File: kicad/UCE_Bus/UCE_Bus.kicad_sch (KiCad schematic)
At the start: 1 part, among them J1 SODIMM-200

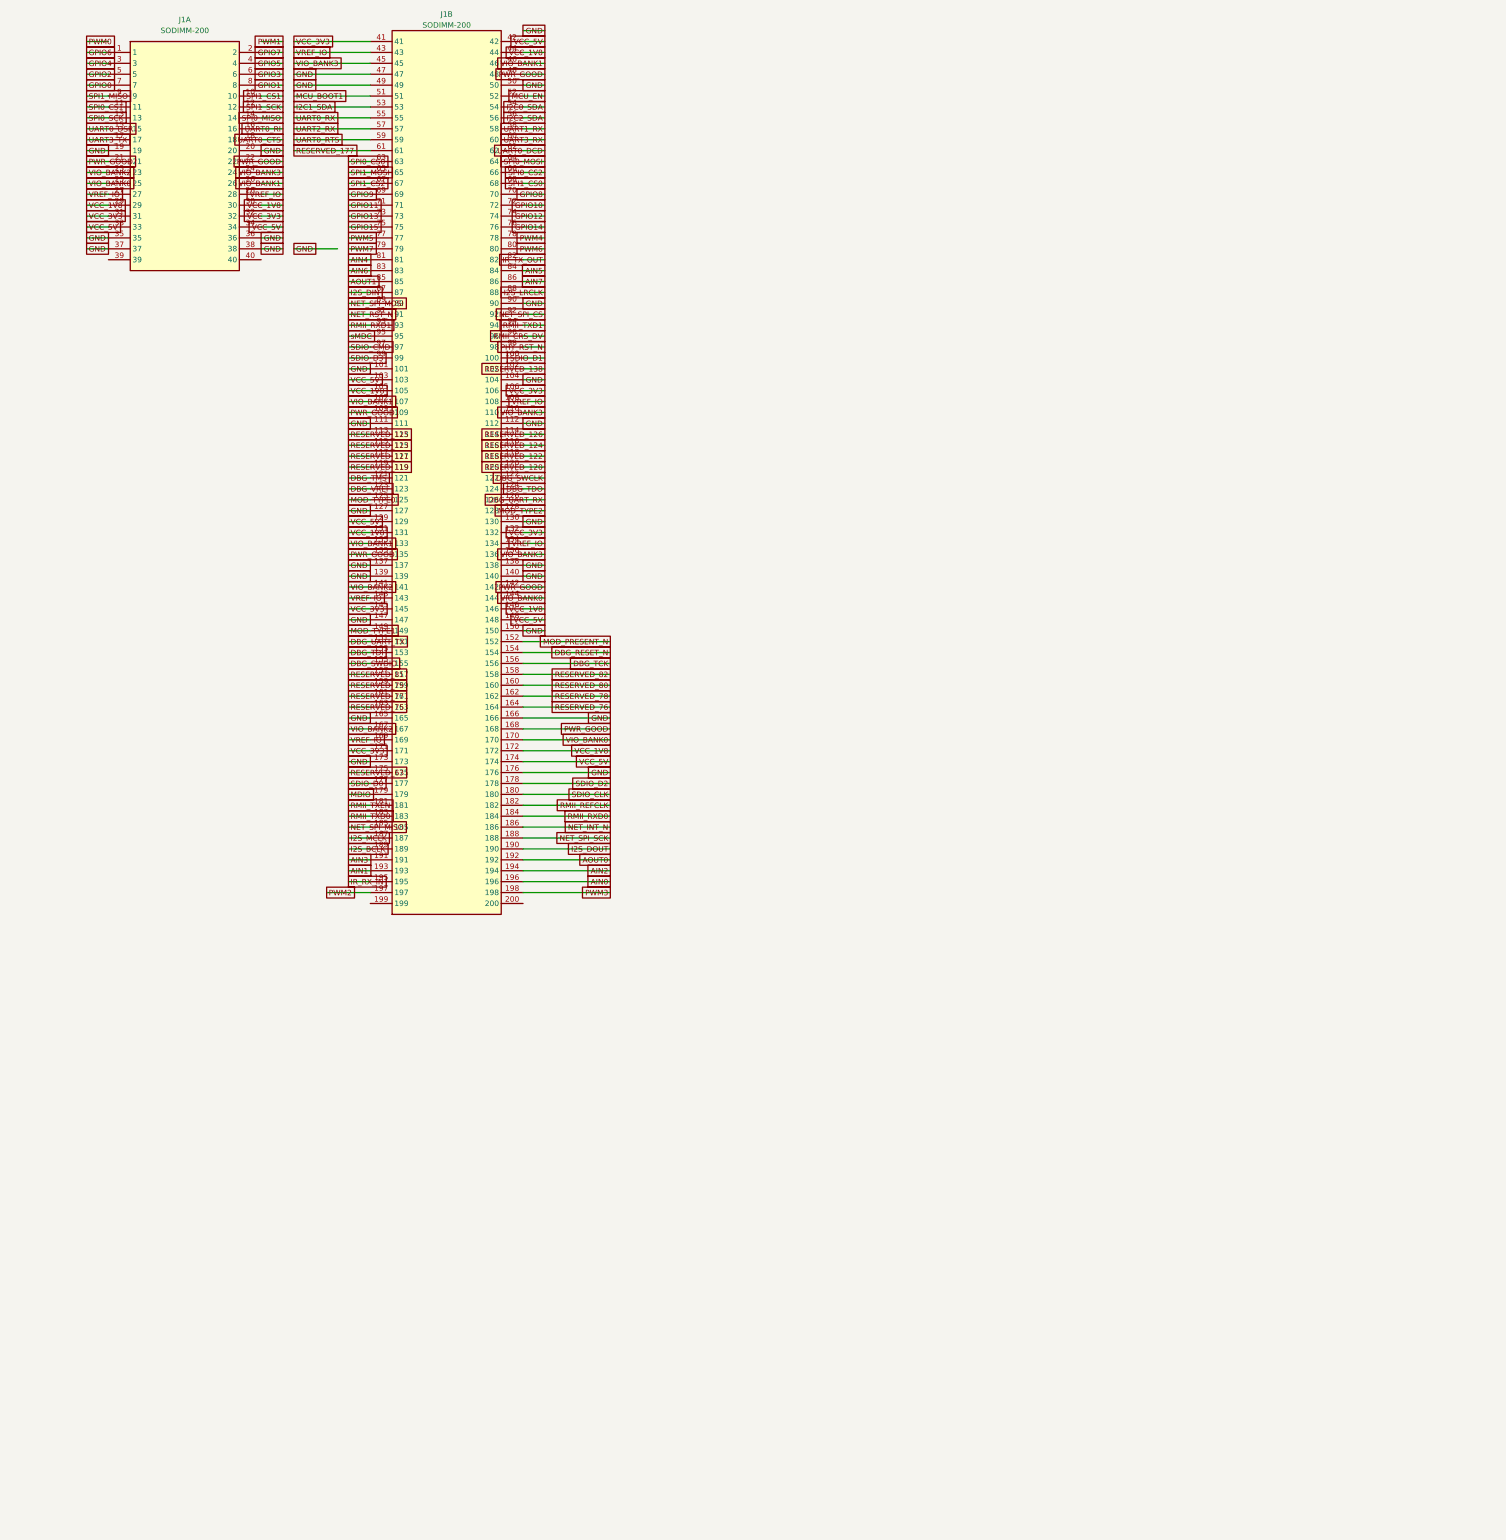
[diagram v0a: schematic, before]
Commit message: Finalizado versão 0.4 do conector do UCE para o módulo.
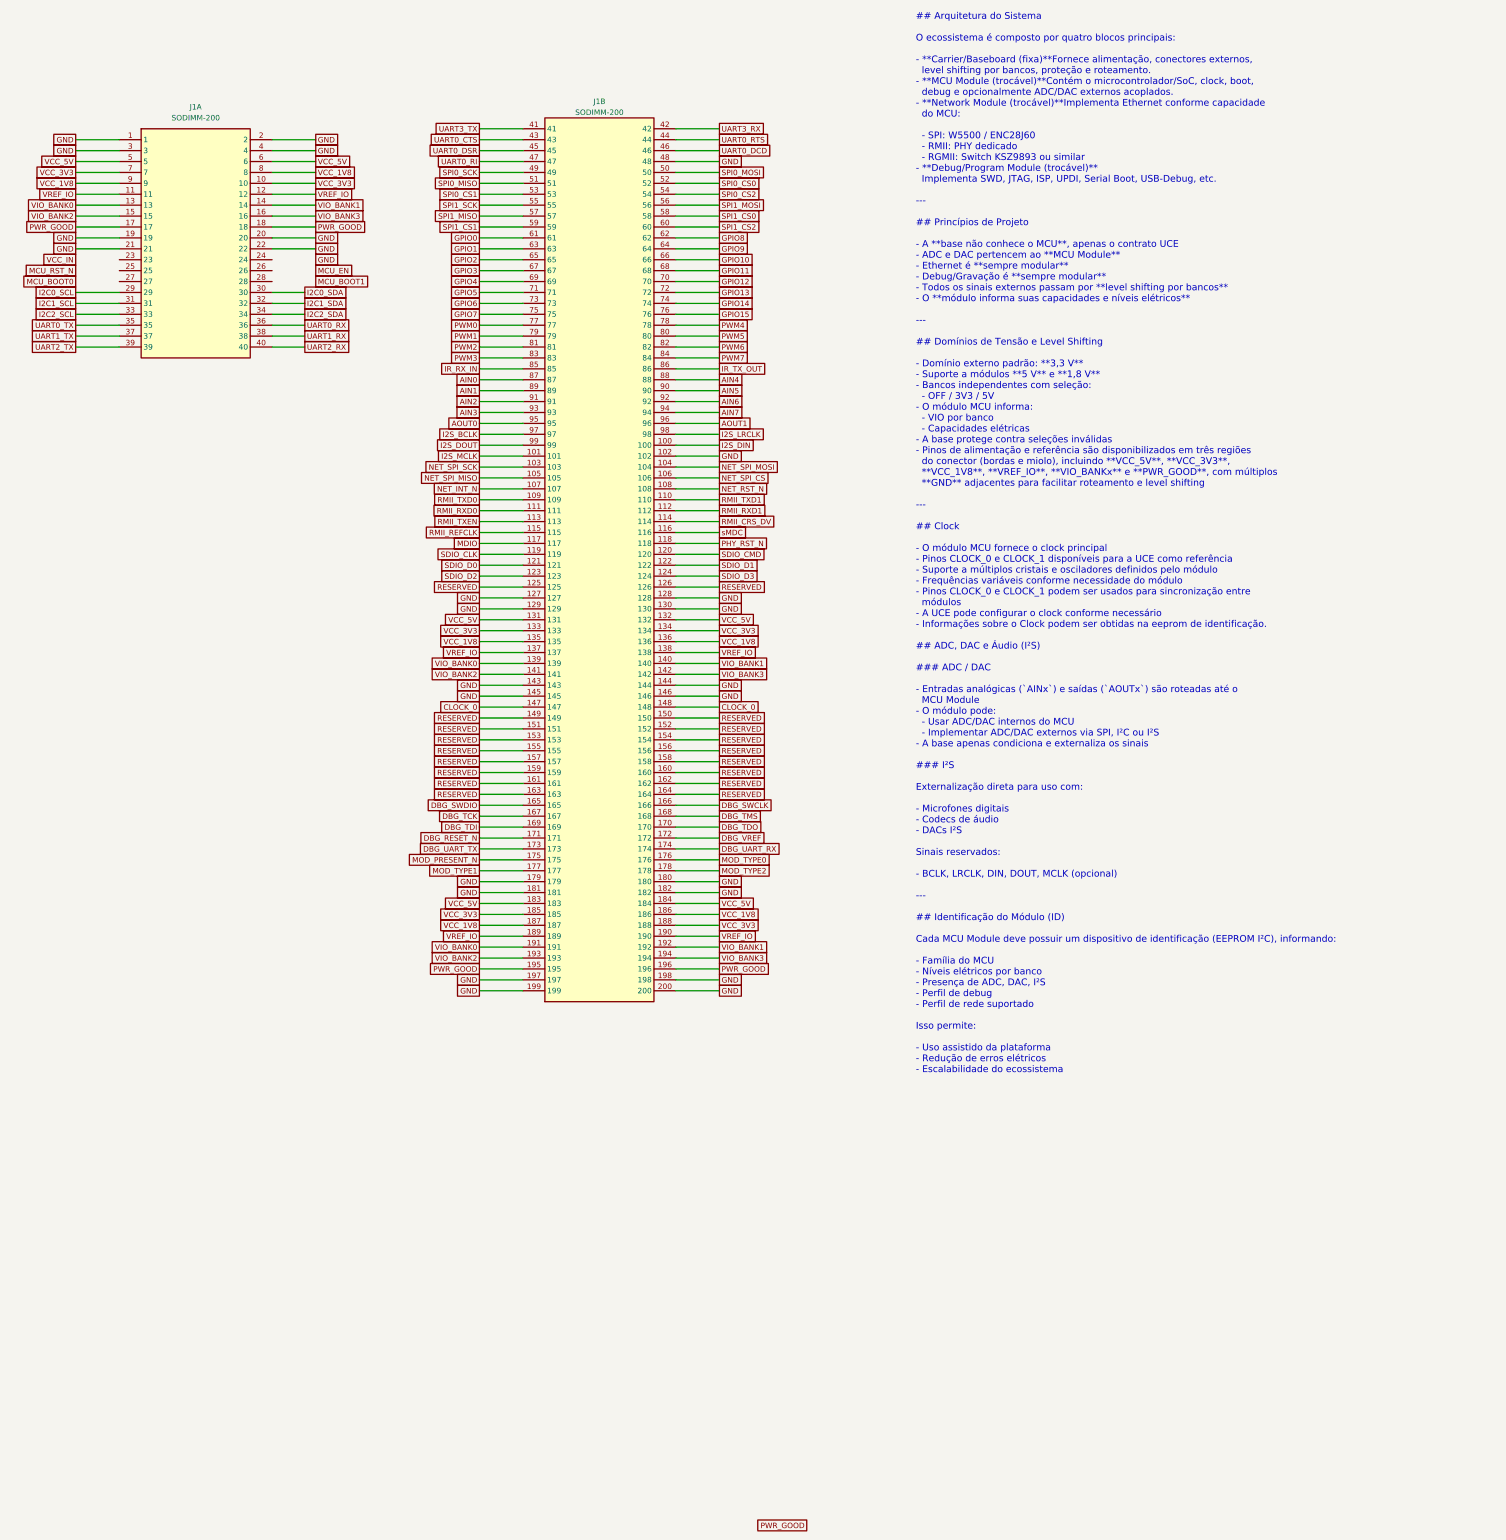
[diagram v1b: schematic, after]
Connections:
- net RESERVED_119 is gone; now on net SDIO_CLK: J1.119
- net RESERVED_120 is gone; now on net SDIO_CMD: J1.120
- net RESERVED_121 is gone; now on net MDIO: J1.117
- net RESERVED_122 is gone; now on net PHY_RST_N: J1.118
- net RESERVED_123 is gone; now on net RMII_REFCLK: J1.115
- net RESERVED_124 is gone; now on net sMDC: J1.116
- net RESERVED_125 is gone; now on net RMII_TXEN: J1.113
- net RESERVED_126 is gone; now on net RMII_CRS_DV: J1.114
- net RESERVED_138 is gone; now on net GND: J1.102
- net RESERVED_177 is gone; now on net GPIO0: J1.61
- net RESERVED_63 is gone; now on net MOD_PRESENT_N: J1.175
- net RESERVED_76 is gone; now on net RESERVED: J1.164
- net RESERVED_77 is gone; now on net RESERVED: J1.161
- net RESERVED_78 is gone; now on net RESERVED: J1.162
- net RESERVED_79 is gone; now on net RESERVED: J1.159
- net RESERVED_80 is gone; now on net RESERVED: J1.160
- net RESERVED_81 is gone; now on net RESERVED: J1.157
- net RESERVED_82 is gone; now on net RESERVED: J1.158
- net AIN0: now also J1.87; no longer J1.196
- net AIN1: now also J1.89; no longer J1.193
- net AIN2: now also J1.91; no longer J1.194
- net AIN3: now also J1.93; no longer J1.191
- net AIN4: now also J1.88; no longer J1.81
- net AIN5: now also J1.90; no longer J1.84
- net AIN6: now also J1.92; no longer J1.83
- net AIN7: now also J1.94; no longer J1.86
- net AOUT0: now also J1.95; no longer J1.192
- net AOUT1: now also J1.96; no longer J1.85
- net DBG_RESET_N: now also J1.171; no longer J1.154
- net DBG_SWCLK: now also J1.166; no longer J1.122
- net DBG_SWDIO: now also J1.165; no longer J1.155
- net DBG_TCK: now also J1.167; no longer J1.156
- net DBG_TDI: now also J1.169; no longer J1.153
- net DBG_TDO: now also J1.170; no longer J1.124
- net DBG_TMS: now also J1.168; no longer J1.121
- net DBG_UART_RX: now also J1.174; no longer J1.126
- net DBG_UART_TX: now also J1.173; no longer J1.151
- net DBG_VREF: now also J1.172; no longer J1.123
- net GND: now also J1.1, J1.128, J1.129, J1.143, J1.144, J1.145, J1.146, J1.179, J1.180, J1.181, J1.182, J1.197, J1.198, J1.199, J1.2, J1.200, J1.21, J1.22, J1.3, J1.4, J1.48; no longer J1.101, J1.104, J1.111, J1.112, J1.137, J1.138, J1.139, J1.140, J1.147, J1.150, J1.165, J1.166, J1.173, J1.176, J1.35, J1.36, J1.37, J1.38, J1.47, J1.49, J1.50, J1.90
- net GPIO0: no longer J1.7
- net GPIO1: now also J1.63; no longer J1.8
- net GPIO10: now also J1.66; no longer J1.72
- net GPIO11: now also J1.68; no longer J1.71
- net GPIO12: now also J1.70; no longer J1.74
- net GPIO13: now also J1.72; no longer J1.73
- net GPIO14: now also J1.74; no longer J1.76
- net GPIO15: now also J1.76; no longer J1.75
- net GPIO2: now also J1.65; no longer J1.5
- net GPIO3: now also J1.67; no longer J1.6
- net GPIO4: now also J1.69; no longer J1.3
- net GPIO5: now also J1.71; no longer J1.4
- net GPIO6: now also J1.73; no longer J1.1
- net GPIO7: now also J1.75; no longer J1.2
- net GPIO8: now also J1.62; no longer J1.70
- net GPIO9: now also J1.64; no longer J1.69
- net I2C0_SDA: now also J1.30; no longer J1.54
- net I2C1_SDA: now also J1.32; no longer J1.53
- net I2C2_SDA: now also J1.34; no longer J1.56
- net I2S_BCLK: now also J1.97; no longer J1.189
- net I2S_DIN: now also J1.100; no longer J1.87
- net I2S_DOUT: now also J1.99; no longer J1.190
- net I2S_LRCLK: now also J1.98; no longer J1.88
- net I2S_MCLK: now also J1.101; no longer J1.187
- net IR_RX_IN: now also J1.85; no longer J1.195
- net IR_TX_OUT: now also J1.86; no longer J1.82
- net MCU_BOOT1: no longer J1.51
- net MCU_EN: no longer J1.52
- net MDIO: no longer J1.179
- net MOD_PRESENT_N: no longer J1.152
- net MOD_TYPE0: now also J1.176; no longer J1.125
- net MOD_TYPE1: now also J1.177; no longer J1.149
- net MOD_TYPE2: now also J1.178; no longer J1.128
- net NET_INT_N: now also J1.107; no longer J1.186
- net NET_RST_N: now also J1.108; no longer J1.91
- net NET_SPI_CS: now also J1.106; no longer J1.92
- net NET_SPI_MISO: now also J1.105; no longer J1.185
- net NET_SPI_MOSI: now also J1.104; no longer J1.89
- net NET_SPI_SCK: now also J1.103; no longer J1.188
- net PHY_RST_N: no longer J1.98
- net PWM0: now also J1.77
- net PWM1: now also J1.79
- net PWM2: now also J1.81; no longer J1.197
- net PWM3: now also J1.83; no longer J1.198
- net PWM5: now also J1.80; no longer J1.77
- net PWM6: now also J1.82; no longer J1.80
- net PWM7: now also J1.84; no longer J1.79
- net PWR_GOOD: now also J1.17, J1.18, J1.195, J1.196; no longer J1.109, J1.135, J1.142, J1.168, J1.21, J1.22, J1.48
- net RMII_CRS_DV: no longer J1.96
- net RMII_REFCLK: no longer J1.182
- net RMII_RXD0: now also J1.111; no longer J1.184
- net RMII_RXD1: now also J1.112; no longer J1.93
- net RMII_TXD0: now also J1.109; no longer J1.183
- net RMII_TXD1: now also J1.110; no longer J1.94
- net RMII_TXEN: no longer J1.181
- net SDIO_CLK: no longer J1.180
- net SDIO_CMD: no longer J1.97
- net SDIO_D0: now also J1.121; no longer J1.177
- net SDIO_D1: now also J1.122; no longer J1.100
- net SDIO_D2: now also J1.123; no longer J1.178
- net SDIO_D3: now also J1.124; no longer J1.99
- net SPI0_CS0: now also J1.52; no longer J1.63
- net SPI0_CS1: now also J1.53; no longer J1.11
- net SPI0_CS2: now also J1.54; no longer J1.66
- net SPI0_MISO: now also J1.51; no longer J1.14
- net SPI0_MOSI: now also J1.50; no longer J1.64
- net SPI0_SCK: now also J1.49; no longer J1.13
- net SPI1_CS0: now also J1.58; no longer J1.68
- net SPI1_CS1: now also J1.59; no longer J1.10
- net SPI1_CS2: now also J1.60; no longer J1.67
- net SPI1_MISO: now also J1.57; no longer J1.9
- net SPI1_MOSI: now also J1.56; no longer J1.65
- net SPI1_SCK: now also J1.55; no longer J1.12
- net UART0_CTS: now also J1.43; no longer J1.18
- net UART0_DCD: now also J1.46; no longer J1.62
- net UART0_DSR: now also J1.45; no longer J1.15
- net UART0_RI: now also J1.47; no longer J1.16
- net UART0_RTS: now also J1.44; no longer J1.59
- net UART0_RX: now also J1.36; no longer J1.55
- net UART1_RX: now also J1.38; no longer J1.58
- net UART2_RX: now also J1.40; no longer J1.57
- net UART3_RX: now also J1.42; no longer J1.60
- net UART3_TX: now also J1.41; no longer J1.17
- net VCC_1V8: now also J1.135, J1.136, J1.186, J1.187, J1.8, J1.9; no longer J1.105, J1.131, J1.146, J1.172, J1.29, J1.30, J1.44
- net VCC_3V3: now also J1.10, J1.133, J1.134, J1.185, J1.188, J1.7; no longer J1.106, J1.132, J1.145, J1.171, J1.31, J1.32, J1.41
- net VCC_5V: now also J1.131, J1.132, J1.183, J1.184, J1.5, J1.6; no longer J1.103, J1.129, J1.148, J1.174, J1.33, J1.34, J1.42
- net VIO_BANK0: now also J1.13, J1.139, J1.191; no longer J1.144, J1.170, J1.25
- net VIO_BANK1: now also J1.14, J1.140, J1.192; no longer J1.107, J1.133, J1.26, J1.46
- net VIO_BANK2: now also J1.15, J1.193; no longer J1.167, J1.23
- net VIO_BANK3: now also J1.142, J1.16, J1.194; no longer J1.110, J1.136, J1.24, J1.45
- net VREF_IO: now also J1.11, J1.12, J1.137, J1.138, J1.189, J1.190; no longer J1.108, J1.134, J1.143, J1.169, J1.27, J1.28, J1.43
- net sMDC: no longer J1.95
- net UART2_TX: now reaches J1.39
- net RESERVED_75 renamed RESERVED
- net RESERVED: now also J1.125, J1.126, J1.149, J1.150, J1.151, J1.152, J1.153, J1.154, J1.155, J1.156
- new net CLOCK_0: J1.147, J1.148
- new net I2C0_SCL: J1.29
- new net I2C1_SCL: J1.31
- new net I2C2_SCL: J1.33
- new net UART0_TX: J1.35
- new net UART1_TX: J1.37
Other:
- note added: "## Arquitetura do Sistema O ecossistema é composto por quatro blocos principais: - **Carrier/Baseboard (fixa)**Fornece alimentação, conectores externos, level shifting por bancos, proteção e roteamento. - **MCU Module (trocável)**Contém o microcontrolador/SoC, clock, boot, debug e opcionalmente ADC/DAC externos acoplados. - **Network Module (trocável)**Implementa Ethernet conforme capacidade do M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"
- company: (none) -> Rapport Tecnologia
- moved on the sheet: J1A, J1B
